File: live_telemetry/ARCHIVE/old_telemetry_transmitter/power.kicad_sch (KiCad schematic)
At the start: 14 parts, among them U3 AP1509-50SG-13, U4 INA180, U5 SPX3819M5-L-3-3/TR

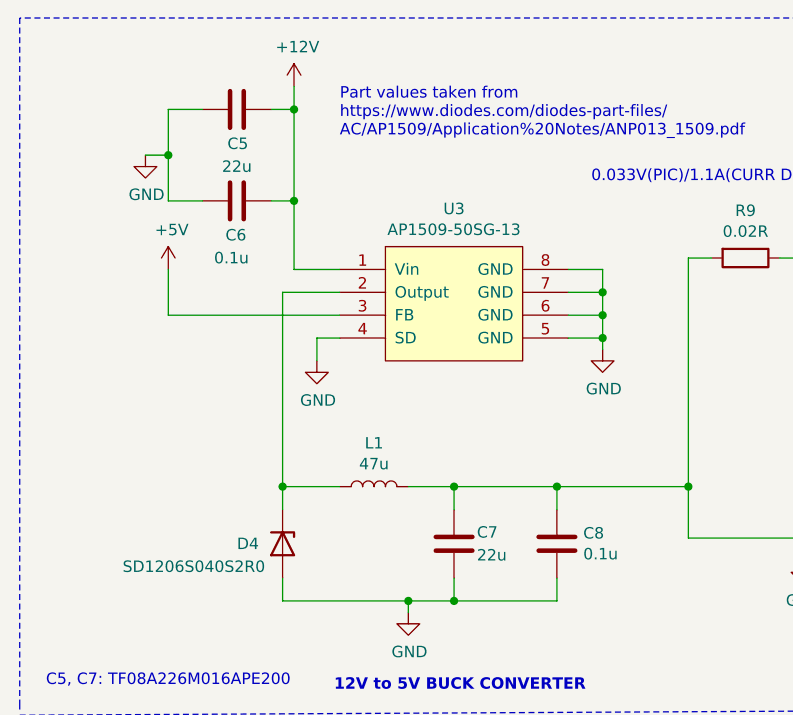
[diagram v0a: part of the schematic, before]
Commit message: add crystal and LDO datasheets, start layout
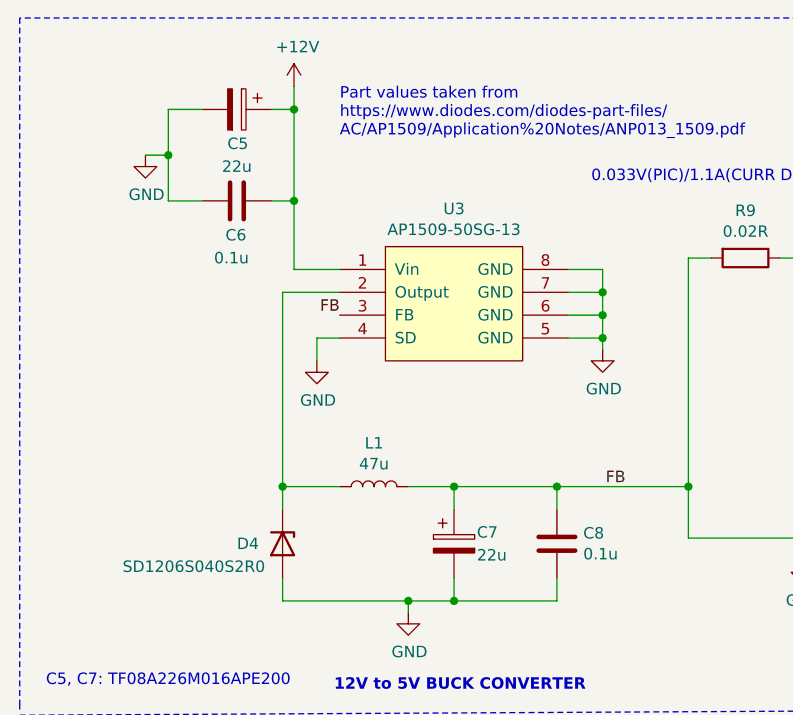
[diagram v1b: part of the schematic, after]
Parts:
- C5, C7: symbol Device:C -> Device:C_Polarized
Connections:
- net +5V: no longer U3.3 (FB)
- net FB: now reaches C7.1, C8.2, L1.2, R9.2, U4.3 (IN+)
- net FB: now also U3.3 (FB)
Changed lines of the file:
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@@
-	(wire
-		(pts
-			(xy 63.5 90.17) (xy 63.5 95.25)
-		)
-		(stroke
-			(width 0)
-			(type default)
-		)
-	)
 	(wire
 		(pts
@@
 	(wire
 		(pts
-			(xy 63.5 95.25) (xy 82.55 95.25)
-		)
-		(stroke
-			(width 0)
-			(type default)
-		)
-	)
-	(wire
-		(pts
 			(xy 107.95 97.79) (xy 111.76 97.79)
 		)
@@
 			(width 0)
 			(type default)
+		)
+	)
+	(label "FB"
+		(at 82.55 95.25 180)
+		(effects
+			(font
+				(size 1.27 1.27)
+			)
+			(justify right bottom)
+		)
+	)
+	(label "FB"
+		(at 114.3 114.3 180)
+		(effects
+			(font
+				(size 1.27 1.27)
+			)
+			(justify right bottom)
 		)
 	)
@@
 	)
 	(symbol
-		(lib_id "power:+5V")
-		(at 63.5 90.17 0)
-		(unit 1)
-		(exclude_from_sim no)
-		(in_bom yes)
-		(on_board yes)
-		(dnp no)
-		(property "Reference" "#PWR023"
-			(at 63.5 93.98 0)
-			(effects
-				(font
-					(size 1.27 1.27)
-				)
-				(hide yes)
-			)
-		)
-		(property "Value" "+5V"
-			(at 63.881 85.7758 0)
-			(effects
-				(font
-					(size 1.27 1.27)
-				)
-			)
-		)
-		(property "Footprint" ""
-			(at 63.5 90.17 0)
-			(effects
-				(font
-					(size 1.27 1.27)
-				)
-				(hide yes)
-			)
-		)
-		(property "Datasheet" ""
-			(at 63.5 90.17 0)
-			(effects
-				(font
-					(size 1.27 1.27)
-				)
-				(hide yes)
-			)
-		)
-		(property "Description" ""
-			(at 63.5 90.17 0)
-			(effects
-				(font
-					(size 1.27 1.27)
-				)
-			)
-		)
-		(pin "1"
-		)
-		(instances
-			(project ""
-				(path "/7ba45e9e-045c-4ae5-8c8c-b5c068df8098/00000000-0000-0000-0000-00005e2687eb"
-					(reference "#PWR023")
-					(unit 1)
-				)
-			)
-		)
-	)
-	(symbol
 		(lib_id "Device:C")
 		(at 71.12 82.55 90)
@@
 	)
 	(symbol
-		(lib_id "Device:C")
+		(lib_id "Device:C_Polarized")
 		(at 71.12 72.39 270)
 		(unit 1)
@@
 			)
 		)
-		(property "Description" "TF08A226M016APE200"
+		(property "Description" "Polarized capacitor"
 			(at 71.12 72.39 0)
 			(effects
@@
 	)
 	(symbol
-		(lib_id "Device:C")
+		(lib_id "Device:C_Polarized")
 		(at 95.25 120.65 0)
 		(unit 1)
@@
 			)
 		)
-		(property "Description" "TF08A226M016APE200"
+		(property "Description" "Polarized capacitor"
 			(at 95.25 120.65 0)
 			(effects

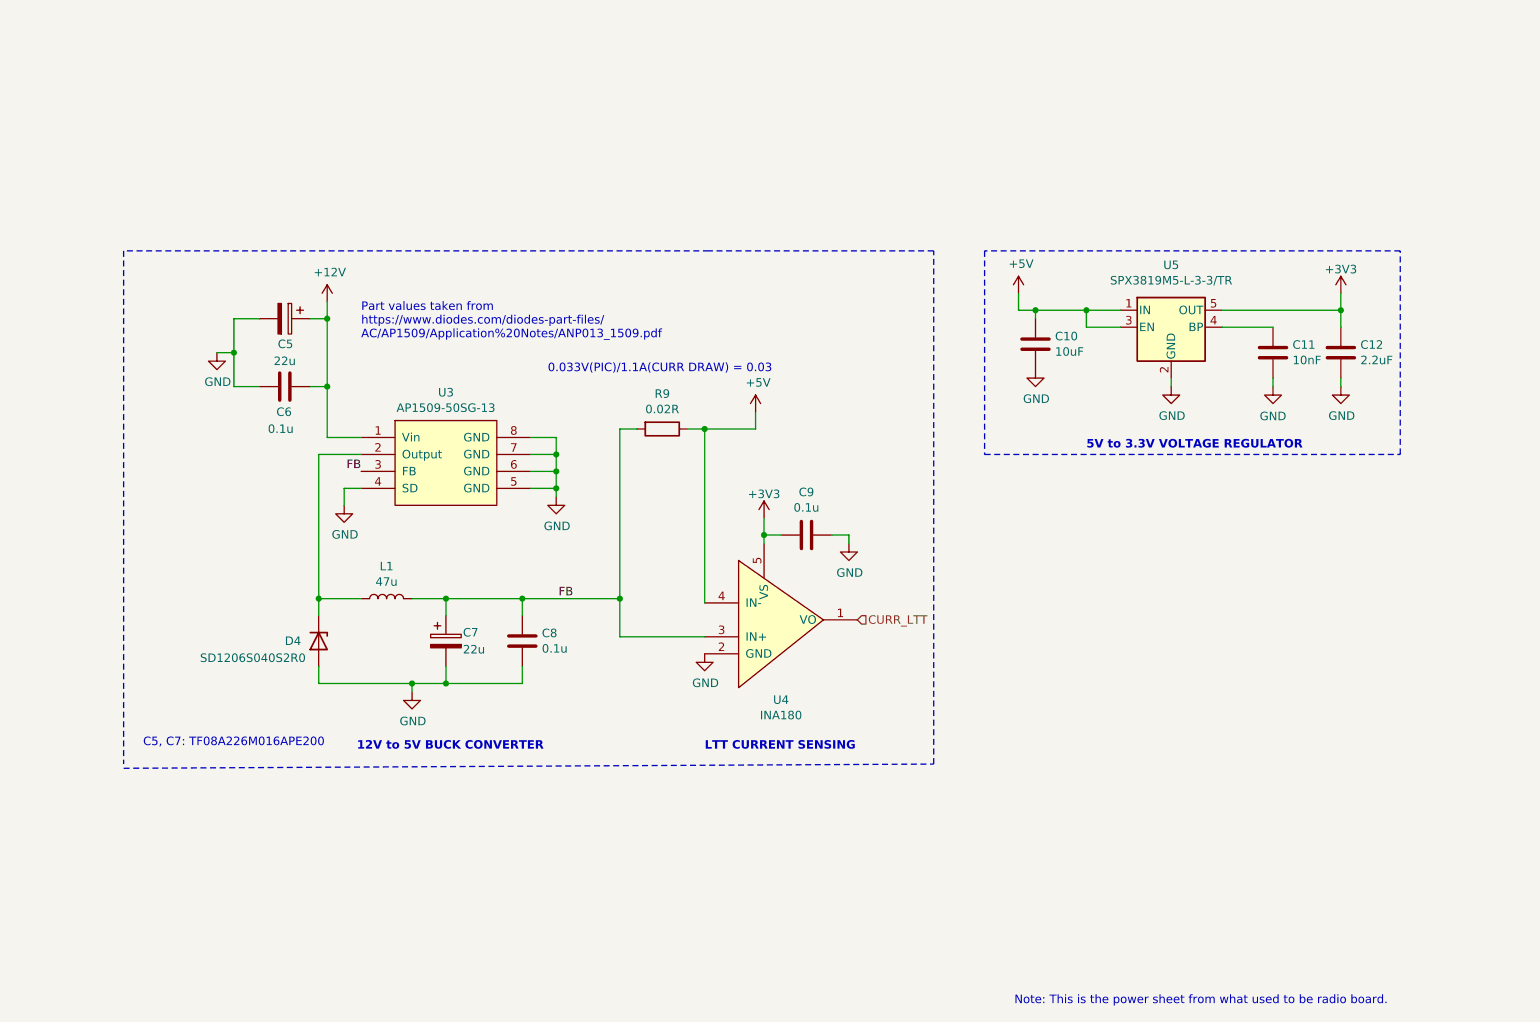
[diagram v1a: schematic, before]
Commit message: finish layout and routing and add 3D models
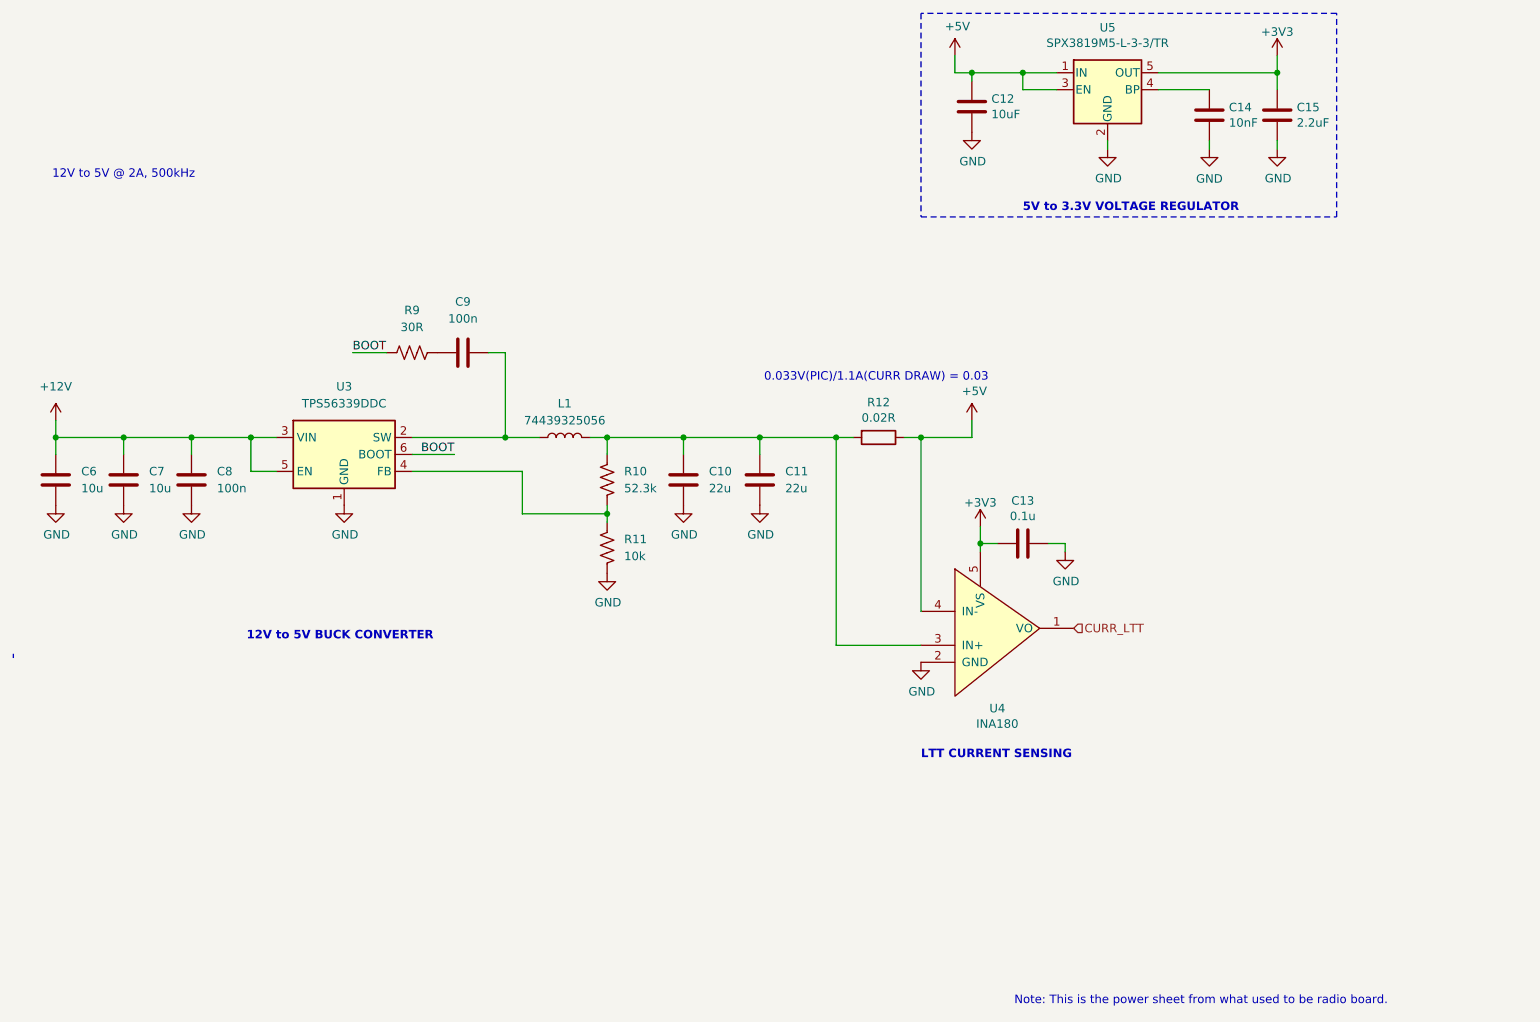
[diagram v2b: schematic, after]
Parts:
- removed C5, C7: 22u, Capacitor_SMD:C_1206_3216Metric_Pad1.33x1.80mm_HandSolder, symbol Device:C_Polarized
- removed D4: SD1206S040S2R0, Diode_SMD:D_1206_3216Metric_Pad1.42x1.75mm_HandSolder, symbol Device:D_Zener
- removed U3: AP1509-50SG-13, Package_SO:SOIC-8_3.9x4.9mm_P1.27mm, symbol canhw:AP1509
- added C10, C11: 22u, Capacitor_SMD:C_0603_1608Metric_Pad1.08x0.95mm_HandSolder, symbol Device:C
- added C7: 10u, Capacitor_SMD:C_0603_1608Metric_Pad1.08x0.95mm_HandSolder, symbol Device:C
- added C9: 100n, Capacitor_SMD:C_0603_1608Metric_Pad1.08x0.95mm_HandSolder, symbol Device:C
- added R10: 52.3k, Resistor_SMD:R_0603_1608Metric_Pad0.98x0.95mm_HandSolder, symbol Device:R_US
- added R11: 10k, Resistor_SMD:R_0603_1608Metric_Pad0.98x0.95mm_HandSolder, symbol Device:R_US
- added R9: 30R, Resistor_SMD:R_0603_1608Metric_Pad0.98x0.95mm_HandSolder, symbol Device:R_US
- added U3: TPS56339DDC, Package_TO_SOT_SMD:SOT-23-6, symbol Regulator_Switching:TPS56339DDC
- C6: value 0.1u -> 10u
- C8: value 0.1u -> 100n
- L1: value 47u -> 74439325056; footprint Inductor_THT:L_Radial_D8.7mm_P5.00mm_Fastron_07HCP -> telemetry_transmitter:WE-XHMI_4040
- renumbered C10 to C12, C9 to C13, C11 to C14, C12 to C15, R9 to R12
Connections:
- net +12V: now also C6.1, C8.1, C7.1, U3.3 (VIN), U3.5 (EN); no longer C6.2
- net GND: now also C6.2, C8.2, C10.2, C11.2, C7.2, R11.2, U3.1 (GND); no longer C6.1, C8.1
- net at L1.1: now also C9.2, U3.2 (SW)
- net FB: no longer names the net of L1.2, R12.2, U4.3 (IN+)
- net FB: now also C10.1, C11.1, R10.1; no longer C8.2
- new net: R10.2, R11.1, U3.4 (FB)
- new net: C9.1, R9.2
- new net BOOT: R9.1, U3.6 (BOOT)
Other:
- note added: "12V to 5V @ 2A, 500kHz"
- note removed: "C5, C7: TF08A226M016APE200"
- note removed: "Part values taken from https://www.diodes.com/diodes-part-files/ AC/AP1509/Application%20Notes/ANP013_1509.pdf"
- moved on the sheet: C12, C13, C14, C15, R12, U4, U5

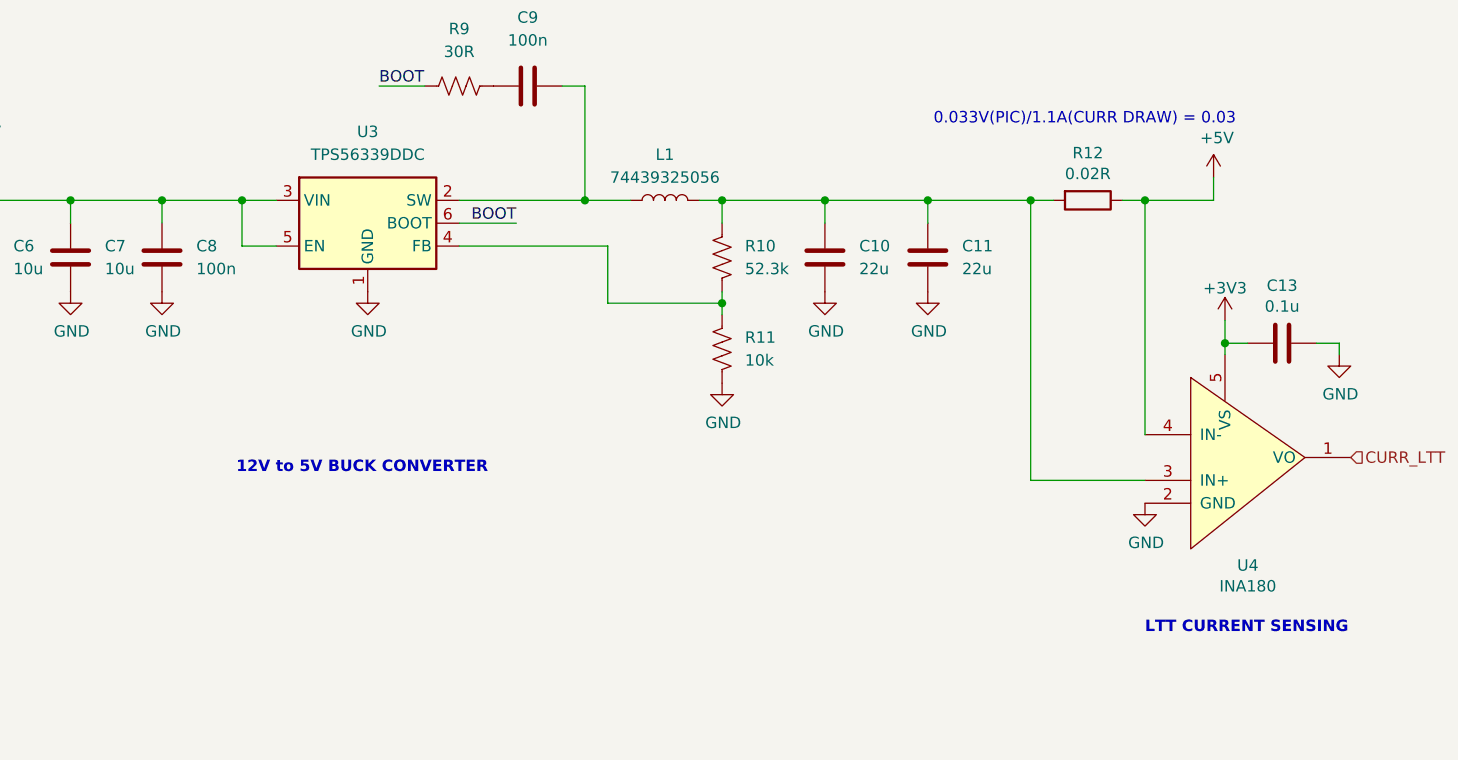
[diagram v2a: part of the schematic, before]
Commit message: minor layout edits, silkscreens placed, logo and board name added, prod files pdf and .step created
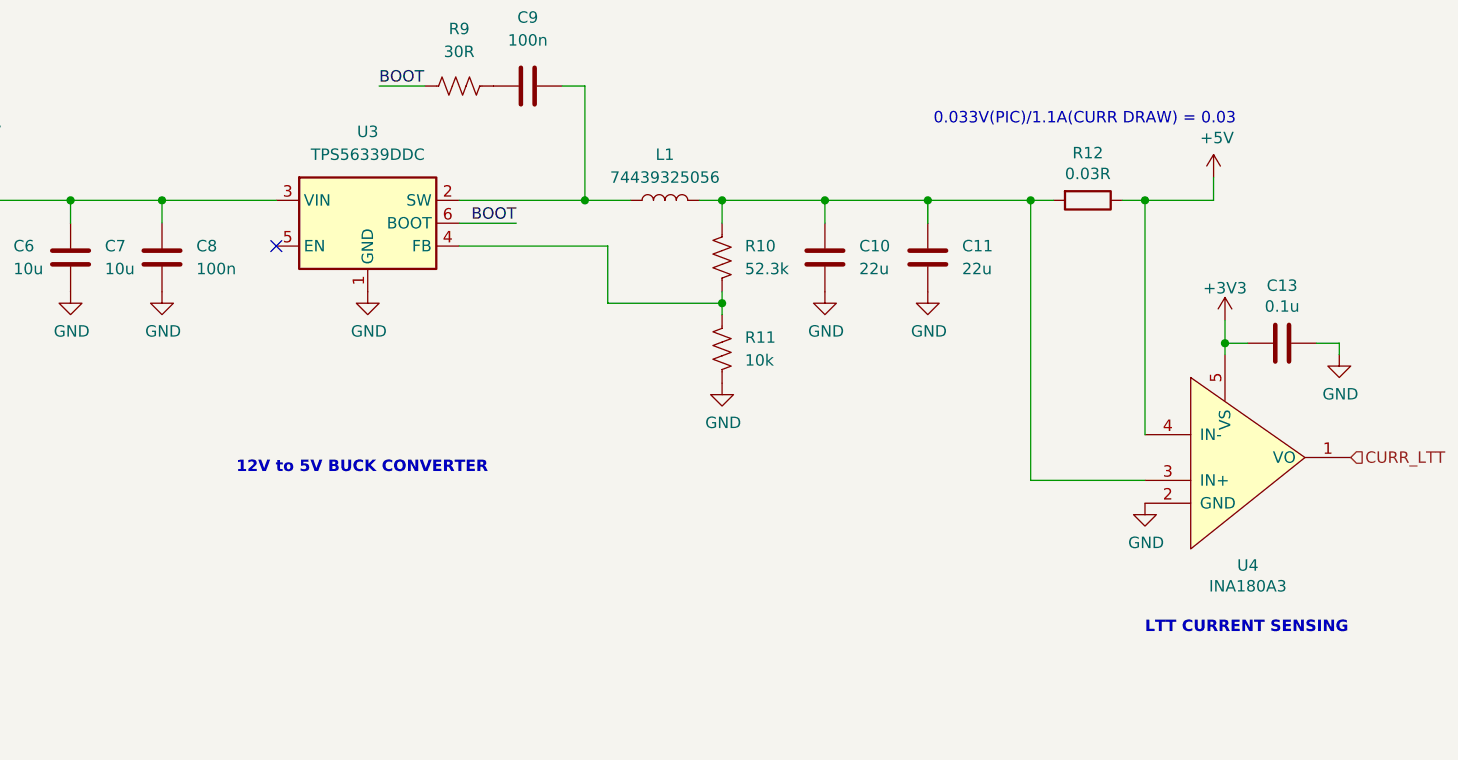
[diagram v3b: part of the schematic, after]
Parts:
- R12: value 0.02R -> 0.03R
- U4: value INA180 -> INA180A3
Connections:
- net +12V: no longer U3.5 (EN)
- no-connect marks 0 -> 1
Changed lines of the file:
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@@
-	)
-	(junction
-		(at 66.04 90.17)
-		(diameter 0)
-		(color 0 0 0 0)
 	)
 	(junction
@@
 		(color 0 0 0 0)
 	)
+	(no_connect
+		(at 69.85 95.25)
+	)
 	(wire
 		(pts
@@
 	(wire
 		(pts
-			(xy 69.85 95.25) (xy 66.04 95.25)
-		)
-		(stroke
-			(width 0)
-			(type default)
-		)
-	)
-	(wire
-		(pts
 			(xy 175.26 106.045) (xy 177.8 106.045)
 		)
@@
 	(wire
 		(pts
-			(xy 66.04 90.17) (xy 66.04 95.25)
-		)
-		(stroke
-			(width 0)
-			(type default)
-		)
-	)
-	(wire
-		(pts
 			(xy 219.71 45.72) (xy 219.71 46.99)
 		)
@@
 	(wire
 		(pts
-			(xy 66.04 90.17) (xy 57.15 90.17)
-		)
-		(stroke
-			(width 0)
-			(type default)
-		)
-	)
-	(wire
-		(pts
 			(xy 175.26 106.045) (xy 175.26 103.505)
 		)
@@
 	(wire
 		(pts
-			(xy 69.85 90.17) (xy 66.04 90.17)
+			(xy 57.15 90.17) (xy 69.85 90.17)
 		)
 		(stroke
@@
 			)
 		)
-		(property "Value" "INA180"
+		(property "Value" "INA180A3"
 			(at 177.8 133.0452 0)
 			(effects
@@
 			)
 		)
-		(property "Value" "0.02R"
+		(property "Value" "0.03R"
 			(at 160.02 87.2236 90)
 			(effects
@@
 			)
 		)
-		(property "Datasheet" "https://www.exar.com/content/document.ashx?id=22106&languageid=1033&type=Datasheet&partnumber=SPX3819&filename=SPX3819.pdf&part=SPX3819"
+		(property "Datasheet" "https://mm.digikey.com/Volume0/opasdata/d220001/medias/docus/6642/1016_SPX3819.pdf"
 			(at 194.31 38.1 0)
 			(effects
@@
 					(size 1.27 1.27)
 				)
-			)
-		)
+				(hide yes)
+			)
+		)
